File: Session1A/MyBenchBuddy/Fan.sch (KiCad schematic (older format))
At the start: 9 parts

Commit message: Understanding the Arduino Module
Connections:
- net Current Measure renamed CURR_MEAS
- net Fan_In renamed FAN_EN_N
- net Power+ renamed FAN_OUT+
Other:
- moved on the sheet: R?, U?
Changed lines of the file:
@@
 LIBS:bth-transistor
 LIBS:bth-converter
+LIBS:bth-ic
 LIBS:MyBenchBuddy-cache
 EELAYER 27 0
@@
 $Descr A4 11693 8268
 encoding utf-8
-Sheet 7 9
+Sheet 9 9
 Title ""
-Date "13 feb 2014"
+Date "26 feb 2014"
 Rev ""
 Comp ""
@@
 Comment4 ""
 $EndDescr
-Text HLabel 6850 2400 0    60   Output ~ 0
-Power+
-Text HLabel 6850 2650 0    60   Input ~ 0
-Power-
-Text HLabel 6850 2850 0    60   Input ~ 0
-Tach
-Text HLabel 1000 4300 0    60   Output ~ 0
-Tach_out
-Text HLabel 850  2800 0    60   Input ~ 0
-Fan_In
+Text HLabel 6850 2400 2    60   Output ~ 0
+FAN_OUT+
+Text HLabel 6850 2650 2    60   Output ~ 0
+FAN_OUT-
+Text HLabel 6850 2850 2    60   Input ~ 0
+TACH_IN
+Text HLabel 1100 4300 0    60   Output ~ 0
+TACH_MEAS
+Text HLabel 1000 2850 0    60   Input ~ 0
+FAN_EN_N
 $Comp
 L LM324 U?
@@
 L MCP4922-E/P U?
 U 1 1 52F6E23B
-P 1500 1950
-F 0 "U?" H 1650 2350 40  0000 L BNN
-F 1 "MCP4922-E/P" H 1650 2300 40  0000 L BNN
-F 2 "DIP14" H 1500 1950 30  0000 C CIN
-F 3 "" H 1500 1950 60  0000 C CNN
-	1    1500 1950
-	1    0    0    -1
-$EndComp
-Wire Wire Line
-	6850 2850 6850 4300
-Wire Wire Line
-	6850 4300 1000 4300
+P 1600 1950
+F 0 "U?" H 1750 2350 40  0000 L BNN
+F 1 "MCP4922-E/P" H 1750 2300 40  0000 L BNN
+F 2 "DIP14" H 1600 1950 30  0000 C CIN
+F 3 "" H 1600 1950 60  0000 C CNN
+	1    1600 1950
+	1    0    0    -1
+$EndComp
+Wire Wire Line
+	6750 4300 1100 4300
 Text HLabel 1300 3000 0    60   Output ~ 0
-Current Measure
+CURR_MEAS
 Wire Wire Line
 	5600 3000 1300 3000
@@
 Connection ~ 3050 1700
 Wire Wire Line
-	3050 2350 3050 2800
-Wire Wire Line
-	3050 2800 850  2800
+	3050 2850 3050 2350
 $Comp
 L R R?
 U 1 1 52F6E630
-P 2400 1800
-F 0 "R?" V 2480 1800 40  0000 C CNN
-F 1 "R" V 2407 1801 40  0000 C CNN
-F 2 "~" V 2330 1800 30  0000 C CNN
-F 3 "~" H 2400 1800 30  0000 C CNN
-	1    2400 1800
+P 2450 1800
+F 0 "R?" V 2530 1800 40  0000 C CNN
+F 1 "R" V 2457 1801 40  0000 C CNN
+F 2 "~" V 2380 1800 30  0000 C CNN
+F 3 "~" H 2450 1800 30  0000 C CNN
+	1    2450 1800
 	0    -1   -1   0
 $EndComp
 Wire Wire Line
-	2150 1800 2050 1800
-Wire Wire Line
-	2650 1800 2750 1800
+	2200 1800 2150 1800
+Wire Wire Line
+	2700 1800 2750 1800
 Connection ~ 2750 1800
 Text HLabel 800  1750 0    60   Input ~ 0
@@
 SCLK
 Wire Wire Line
-	950  1750 800  1750
-Wire Wire Line
-	950  1850 800  1850
-Wire Wire Line
-	950  1950 800  1950
+	1050 1750 800  1750
+Wire Wire Line
+	1050 1850 800  1850
+Wire Wire Line
+	1050 1950 800  1950
 $Comp
 L R R?
 U 1 1 52F6E833
-P 950 2450
-F 0 "R?" V 1030 2450 40  0000 C CNN
-F 1 "R" V 957 2451 40  0000 C CNN
-F 2 "~" V 880 2450 30  0000 C CNN
-F 3 "~" H 950 2450 30  0000 C CNN
-	1    950  2450
+P 1050 2450
+F 0 "R?" V 1130 2450 40  0000 C CNN
+F 1 "R" V 1057 2451 40  0000 C CNN
+F 2 "~" V 980 2450 30  0000 C CNN
+F 3 "~" H 1050 2450 30  0000 C CNN
+	1    1050 2450
 	-1   0    0    1
 $EndComp
 Wire Wire Line
-	950  2150 950  2200
-Wire Wire Line
-	950  2700 950  2800
-Connection ~ 950  2800
+	1050 2150 1050 2200
+Wire Wire Line
+	6750 4300 6750 2850
+Wire Wire Line
+	6750 2850 6850 2850
+Wire Wire Line
+	1050 2700 1050 2850
+Wire Wire Line
+	1000 2850 3050 2850
+Connection ~ 1050 2850
 $EndSCHEMATC

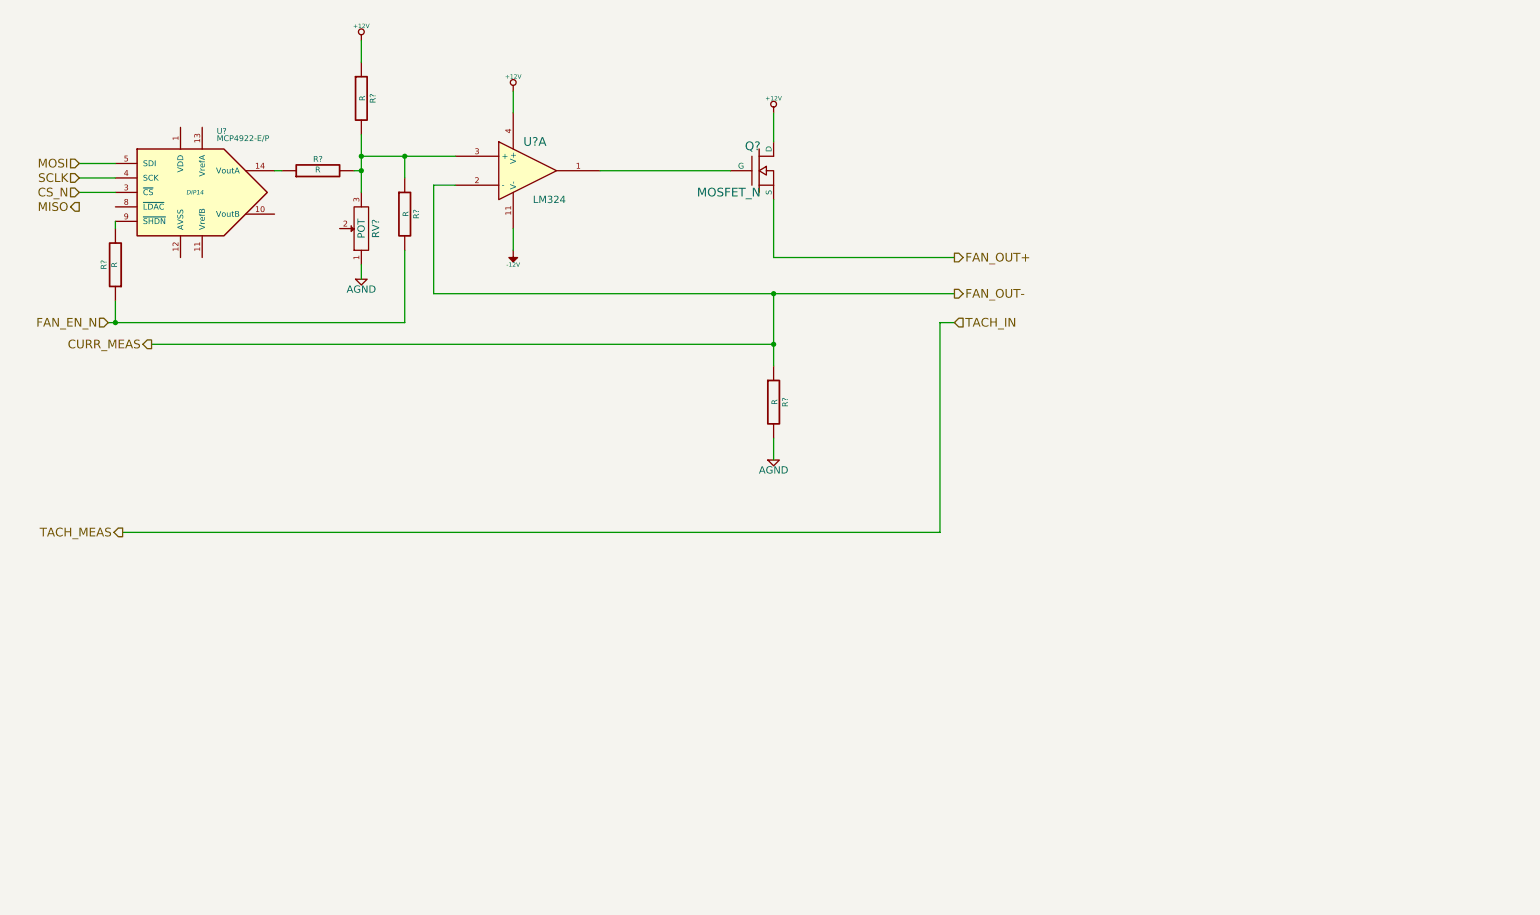
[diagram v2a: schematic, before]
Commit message: Revisiting The Current/Fan Module
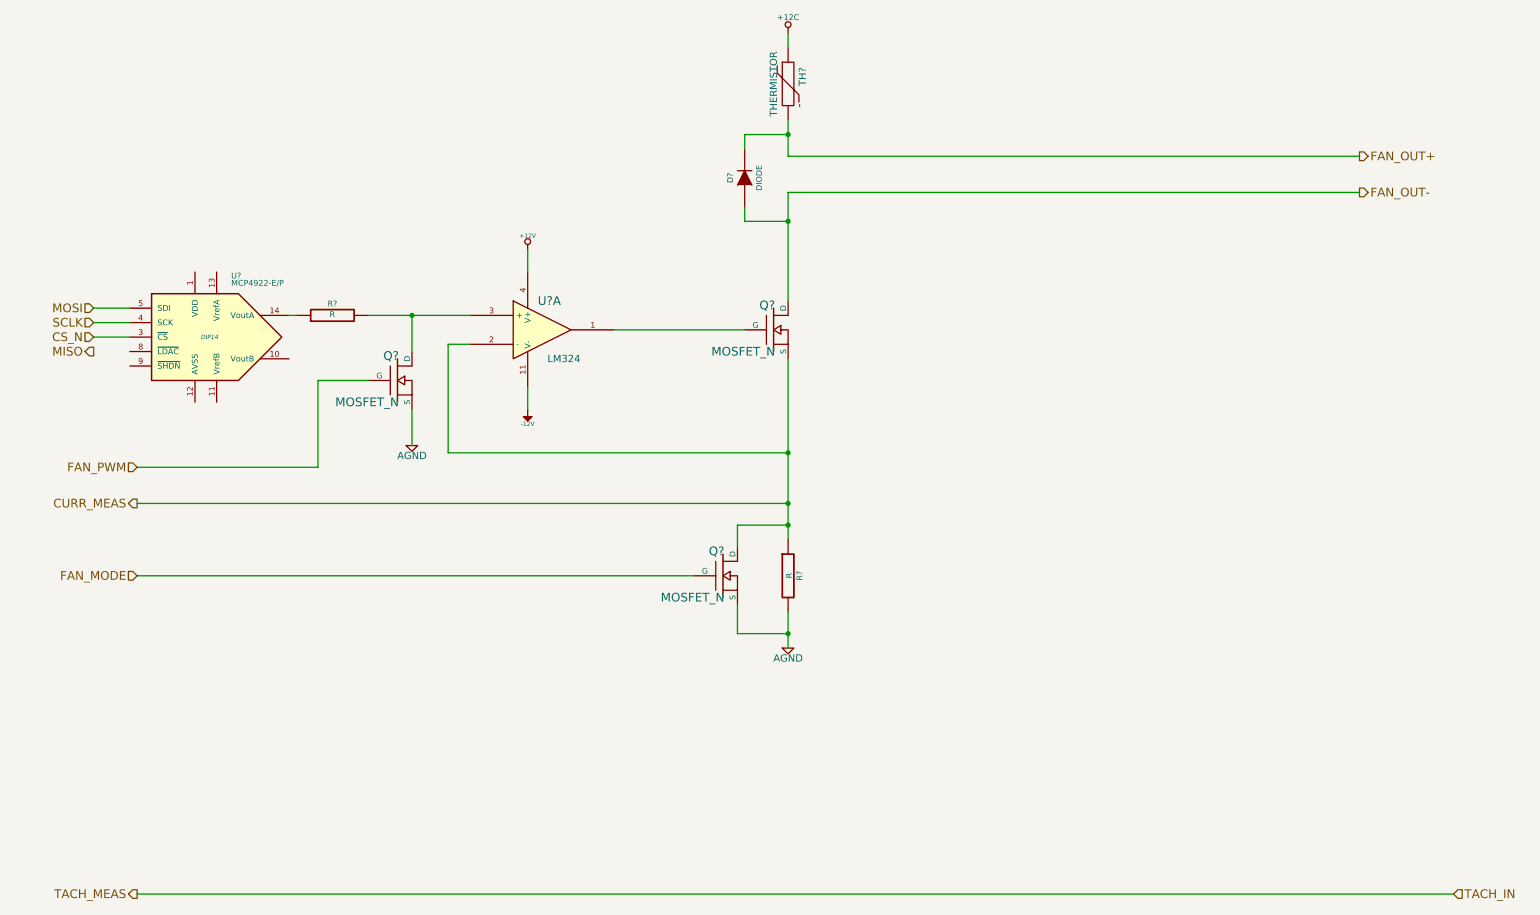
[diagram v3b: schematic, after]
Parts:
- removed R? (x3): R, ~, symbol R
- removed RV?: POT, ~, symbol POT
- added D?: DIODE, ~, symbol DIODE
- added Q? (x2): MOSFET_N, ~, symbol MOSFET_N
- added TH?: THERMISTOR, ~, symbol THERMISTOR
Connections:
- net +12V: no longer Q?.D
- net AGND: now also Q?.S, Q?.S
- net CURR_MEAS: now also Q?.S, Q?.D
- net FAN_OUT+: now also D?.2 (K), TH?.2; no longer Q?.S
- net at R?.2, U?.3 (+): now also Q?.D
- new net +12C: TH?.1
- new net FAN_MODE: Q?.G
- new net FAN_OUT-: D?.1 (A), Q?.D
- new net FAN_PWM: Q?.G
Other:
- moved on the sheet: Q?, R?, U?, U?A

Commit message: initial
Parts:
- U11: renamed from U?; value LM324 -> OPA4170
- gave numbers to parts that had none: 8
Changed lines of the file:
@@
 Sheet 6 9
 Title ""
-Date "1 mar 2014"
+Date "15 mar 2014"
 Rev ""
 Comp ""
@@
 FAN_PWM
 $Comp
-L LM324 U?
+L LM324 U11
 U 1 1 52F6DE8C
 P 4000 2900
-F 0 "U?" H 4050 3100 60  0000 C CNN
-F 1 "LM324" H 4150 2700 50  0000 C CNN
+F 0 "U11" H 4050 3100 60  0000 C CNN
+F 1 "OPA4170" H 4150 2700 50  0000 C CNN
 F 2 "" H 4000 2900 60  0000 C CNN
 F 3 "" H 4000 2900 60  0000 C CNN
@@
 $EndComp
 $Comp
-L MOSFET_N Q?
+L MOSFET_N Q4
 U 1 1 52F6DEAA
 P 5600 2900
-F 0 "Q?" H 5610 3070 60  0000 R CNN
+F 0 "Q4" H 5610 3070 60  0000 R CNN
 F 1 "MOSFET_N" H 5610 2750 60  0000 R CNN
 F 2 "~" H 5600 2900 60  0000 C CNN
@@
 $EndComp
 $Comp
-L R R?
+L R R20
 U 1 1 52F6DECF
 P 5700 4600
-F 0 "R?" V 5780 4600 40  0000 C CNN
+F 0 "R20" V 5780 4600 40  0000 C CNN
 F 1 "R" V 5707 4601 40  0000 C CNN
 F 2 "~" V 5630 4600 30  0000 C CNN
@@
 	5400 2900 4500 2900
 Wire Wire Line
-	5700 3100 5700 3750
-Wire Wire Line
-	5700 3750 5700 4100
-Wire Wire Line
-	5700 4100 5700 4250
-Wire Wire Line
-	5700 4250 5700 4350
-$Comp
-L AGND #PWR?
+	5700 3100 5700 4350
+$Comp
+L AGND #PWR39
 U 1 1 52F6DF73
 P 5700 5100
-F 0 "#PWR?" H 5700 5100 40  0001 C CNN
+F 0 "#PWR39" H 5700 5100 40  0001 C CNN
 F 1 "AGND" H 5700 5030 50  0000 C CNN
 F 2 "" H 5700 5100 60  0000 C CNN
@@
 $EndComp
 Wire Wire Line
-	5700 4850 5700 5000
-Wire Wire Line
-	5700 5000 5700 5100
+	5700 4850 5700 5100
 Wire Wire Line
 	3350 3750 3350 3000
@@
 Connection ~ 5700 3750
 $Comp
-L +12V #PWR?
+L +12V #PWR36
 U 1 1 52F6E01A
 P 3900 2350
-F 0 "#PWR?" H 3900 2300 20  0001 C CNN
+F 0 "#PWR36" H 3900 2300 20  0001 C CNN
 F 1 "+12V" H 3900 2450 30  0000 C CNN
 F 2 "" H 3900 2350 60  0000 C CNN
@@
 	3900 2350 3900 2500
 Wire Wire Line
-	5700 1950 5700 2150
-Wire Wire Line
-	5700 2150 5700 2700
-$Comp
-L -12V #PWR?
+	5700 1950 5700 2700
+$Comp
+L -12V #PWR37
 U 1 1 52F6E035
 P 3900 3450
-F 0 "#PWR?" H 3900 3580 20  0001 C CNN
+F 0 "#PWR37" H 3900 3580 20  0001 C CNN
 F 1 "-12V" H 3900 3550 30  0000 C CNN
 F 2 "" H 3900 3450 60  0000 C CNN
@@
 	3900 3300 3900 3450
 $Comp
-L AGND #PWR?
+L AGND #PWR35
 U 1 1 52F6E17E
 P 3100 3700
-F 0 "#PWR?" H 3100 3700 40  0001 C CNN
+F 0 "#PWR35" H 3100 3700 40  0001 C CNN
 F 1 "AGND" H 3100 3630 50  0000 C CNN
 F 2 "" H 3100 3700 60  0000 C CNN
@@
 $EndComp
 $Comp
-L MCP4922-E/P U?
+L MCP4922-E/P U8
 U 1 1 52F6E23B
 P 1700 2950
-F 0 "U?" H 1850 3350 40  0000 L BNN
+F 0 "U8" H 1850 3350 40  0000 L BNN
 F 1 "MCP4922-E/P" H 1850 3300 40  0000 L BNN
 F 2 "DIP14" H 1700 2950 30  0000 C CIN
@@
 Connection ~ 5700 4100
 $Comp
-L R R?
+L R R19
 U 1 1 52F6E630
 P 2550 2800
-F 0 "R?" V 2630 2800 40  0000 C CNN
+F 0 "R19" V 2630 2800 40  0000 C CNN
 F 1 "R" V 2557 2801 40  0000 C CNN
 F 2 "~" V 2480 2800 30  0000 C CNN
@@
 	1150 2950 900  2950
 $Comp
-L MOSFET_N Q?
+L MOSFET_N Q3
 U 1 1 53114F50
 P 5250 4600
-F 0 "Q?" H 5260 4770 60  0000 R CNN
+F 0 "Q3" H 5260 4770 60  0000 R CNN
 F 1 "MOSFET_N" H 5260 4450 60  0000 R CNN
 F 2 "~" H 5250 4600 60  0000 C CNN
@@
 $EndComp
 $Comp
-L THERMISTOR TH?
+L THERMISTOR TH5
 U 1 1 531151BE
 P 5700 1200
-F 0 "TH?" V 5800 1250 50  0000 C CNN
+F 0 "TH5" V 5800 1250 50  0000 C CNN
 F 1 "THERMISTOR" V 5600 1200 50  0000 C CNN
 F 2 "~" H 5700 1200 60  0000 C CNN
@@
 	5700 850  5700 950
 Wire Wire Line
-	5700 1450 5700 1550
-Wire Wire Line
-	5700 1550 5700 1700
+	5700 1450 5700 1700
 Wire Wire Line
 	5700 1700 9650 1700
@@
 	5700 1950 9650 1950
 $Comp
-L DIODE D?
+L DIODE D4
 U 1 1 531156FB
 P 5400 1850
-F 0 "D?" H 5400 1950 40  0000 C CNN
+F 0 "D4" H 5400 1950 40  0000 C CNN
 F 1 "DIODE" H 5400 1750 40  0000 C CNN
 F 2 "~" H 5400 1850 60  0000 C CNN
@@
 	1200 3850 2450 3850
 Wire Wire Line
-	2800 2800 3100 2800
-Wire Wire Line
-	3100 2800 3500 2800
-$Comp
-L MOSFET_N Q?
+	2800 2800 3500 2800
+$Comp
+L MOSFET_N Q2
 U 1 1 53116E55
 P 3000 3250
-F 0 "Q?" H 3010 3420 60  0000 R CNN
+F 0 "Q2" H 3010 3420 60  0000 R CNN
 F 1 "MOSFET_N" H 3010 3100 60  0000 R CNN
 F 2 "~" H 3000 3250 60  0000 C CNN
@@
 	5050 4600 1200 4600
 $Comp
-L +12C #PWR?
+L +12C #PWR38
 U 1 1 53119095
 P 5700 850
-F 0 "#PWR?" H 5700 820 30  0001 C CNN
+F 0 "#PWR38" H 5700 820 30  0001 C CNN
 F 1 "+12C" H 5700 960 40  0000 C CNN
 F 2 "" H 5700 850 60  0000 C CNN
